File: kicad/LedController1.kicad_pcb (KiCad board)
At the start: 2 copper layers, 20 x 100 mm, 15 parts, among them J1 AudioJack2, J2 AudioJack2, J3 AudioJack2, J4 EURO_PWR_2x5-eurocad-euro_pwr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, J5 Conn_01x04_Female, U1 TL084

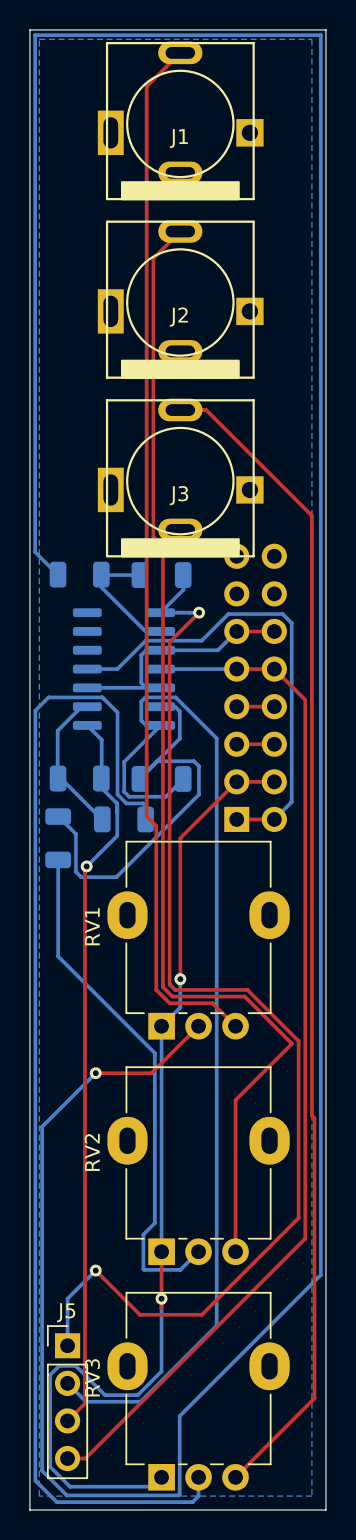
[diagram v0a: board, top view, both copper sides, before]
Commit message: Correcting PJ301BM footprint
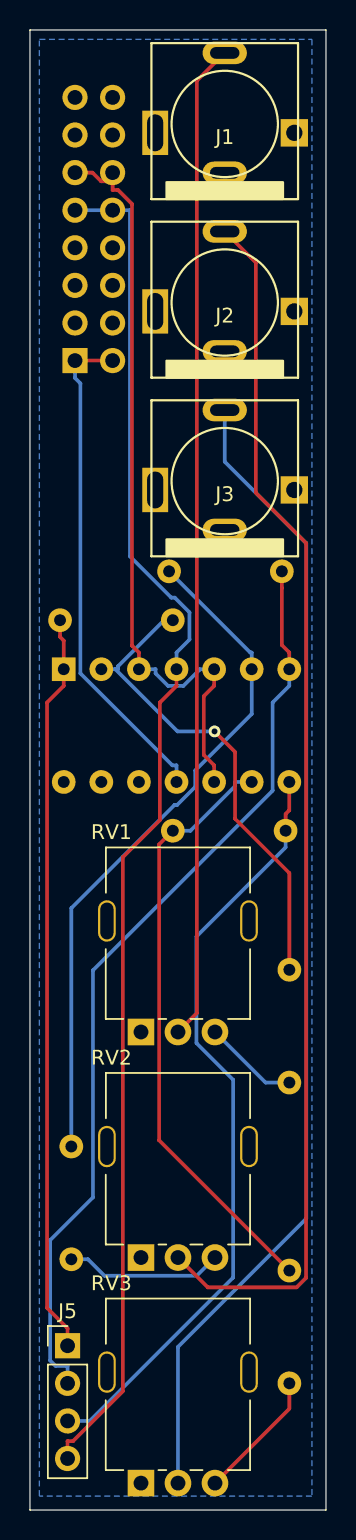
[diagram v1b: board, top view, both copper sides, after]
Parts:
- J1, J2, J3: footprint SynthDiyFootprintLibrary:PJ301BM -> SynthDiy:PJ301BM
- J4: value EURO_PWR_2x5-eurocad-euro_pwr_2x5-eurocad -> Conn_02x08_Odd_Even
- R1, R2, R3, R4, R5, R6: footprint Resistor_SMD:R_1206_3216Metric -> SynthDiy:R_Axial_DIN0207_L6.3mm_D2.5mm_P7.62mm_Horizontal
- RV1, RV2, RV3: footprint Potentiometer_THT:Potentiometer_Alpha_RD901F-40-00D_Single_Vertical -> SynthDiy:Potentiometer_Alpha_Single_Vertical
- U1: footprint Package_SO:SOIC-14_3.9x8.7mm_P1.27mm -> Package_DIP:DIP-14_W7.62mm_Socket
- moved J4 32.9 mm to (3.04, 22.3)
- moved R3 32.5 mm to (17.5, 83.8), turned to -90 degrees
- moved R1 30.2 mm to (17.5, 63.5), turned to -90 degrees
- moved R2 20.8 mm to (2.79, 75.4)
- moved R5 14.0 mm to (9.40, 36.6)
- moved R6 7.21 mm to (9.65, 54.1)
- moved RV3 7.20 mm to (10.0, 90.7)
- moved RV1 7.20 mm to (10.0, 60.2)
- moved RV2 7.20 mm to (10.0, 75.4)
- moved U1 4.07 mm to (2.28, 43.2), turned to -90 degrees
- moved R4 3.14 mm to (9.65, 39.9), turned to 180 degrees
- moved J1 3.00 mm to (13.2, 6.35)
- moved J2 3.00 mm to (13.2, 18.4)
- moved J3 3.00 mm to (13.2, 30.5)
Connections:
- J4 pad 13: (no net) -> unconnected-(J4-Pad13)
- J4 pad 14: (no net) -> unconnected-(J4-Pad14)
- J4 pad 15: (no net) -> unconnected-(J4-Pad15)
- J4 pad 16: (no net) -> unconnected-(J4-Pad16)
- RV1 pad 2: /InputSignal/Signal -> Net-(J1-PadT)
- RV1 pad 3: Net-(J1-PadT) -> /InputSignal/Signal
- RV2 pad 2: /sheet5FE679DC/Signal -> Net-(J2-PadT)
- RV2 pad 3: Net-(J2-PadT) -> /sheet5FE679DC/Signal
- RV3 pad 2: /sheet5FE67A34/Signal -> Net-(J3-PadT)
- RV3 pad 3: Net-(J3-PadT) -> /sheet5FE67A34/Signal
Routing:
- net /InputSignal/Signal: track 205.6 -> 6.44 mm, vias 1 -> 0
- net GND: track 74.0 -> 0.00 mm, vias 2 -> 0
- net /sheet5FE67A34/Signal: track 80.2 -> 8.82 mm
- net +5V: track 17.9 -> 51.7 mm
- net Net-(R3-Pad1): track 10.0 -> 40.6 mm
- net Net-(J5-Pad1): track 77.5 -> 50.2 mm, vias 2 -> 0
- net Net-(R1-Pad1): track 8.65 -> 33.0 mm, vias 0 -> 1
- net +12V: track 69.2 -> 93.5 mm
- net /sheet5FE679DC/Signal: track 34.9 -> 10.7 mm
- net Net-(R2-Pad1): track 28.7 -> 46.4 mm
- net Net-(J5-Pad2): track 71.6 -> 62.7 mm
- net Net-(J2-PadT): track 78.0 -> 82.7 mm
- net Net-(J1-PadT): track 70.9 -> 67.5 mm
- net Net-(J5-Pad3): track 49.6 -> 52.3 mm, vias 1 -> 0
- net -12V: track 31.9 -> 34.0 mm
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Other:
- net class Default removed
- board text added: "OldManModular CV-LED rev 3"
- board text removed: "OldManModular CV-LED rev 2"
